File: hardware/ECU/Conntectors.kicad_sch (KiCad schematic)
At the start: 1 part

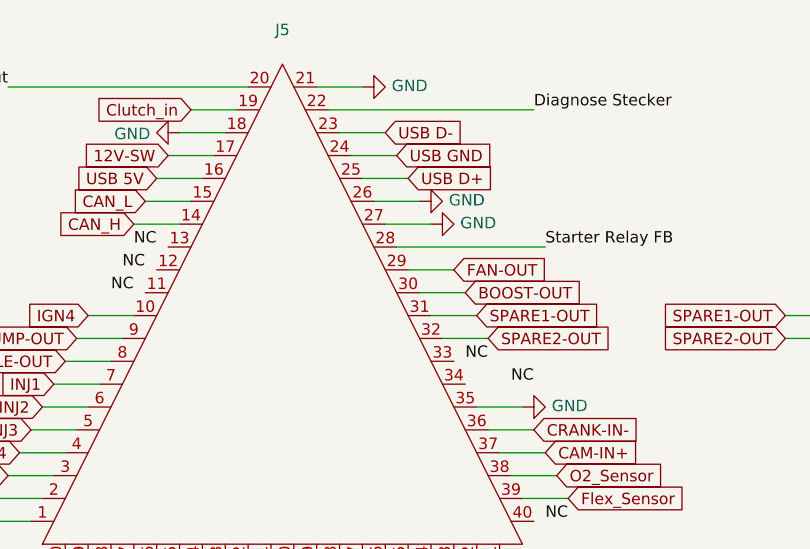
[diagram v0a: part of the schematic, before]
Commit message: Replace speeduino submodule with HasiKe fork, fix teensy.pretty path
- Switch speeduino from speeduino/speeduino to HasiKe/speeduino
- Fix teensy.pretty submodule path case mismatch (Hardware -> hardware)
- Add ISL9V5036P3-F085 component library
- Various ECU schematic updates
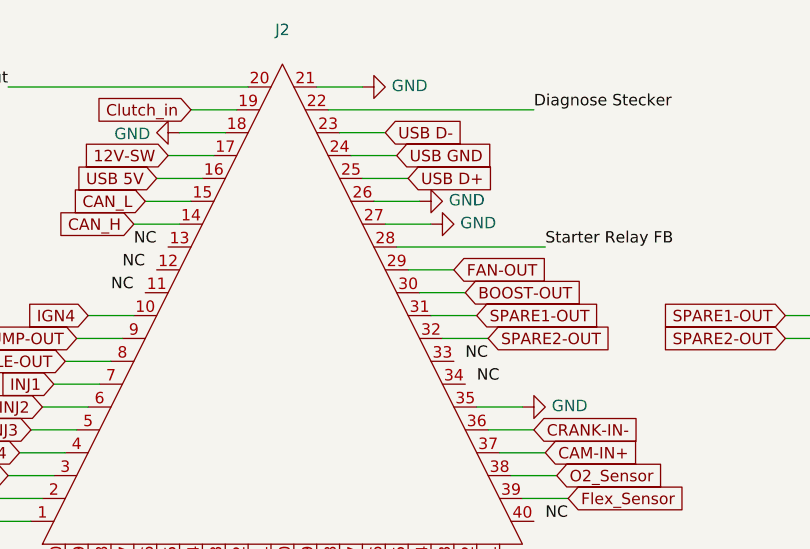
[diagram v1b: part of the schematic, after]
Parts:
- renumbered J5 to J2
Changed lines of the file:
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@@
 	)
 	(label "NC"
-		(at 173.99 99.06 0)
+		(at 170.18 99.06 0)
 		(effects
 			(font
@@
 		(on_board yes)
 		(dnp no)
-		(property "Reference" "#PWR0132"
+		(property "Reference" "#PWR031"
 			(at 181.61 101.6 0)
 			(effects
@@
 			(project "ECU"
 				(path "/aaebd8f9-fdac-426b-87c0-a208167b6035/a9903762-e61d-4762-913c-0f836ea1045d"
-					(reference "#PWR0132")
+					(reference "#PWR031")
 					(unit 1)
 				)
@@
 		(on_board yes)
 		(dnp no)
-		(property "Reference" "#PWR019"
+		(property "Reference" "#PWR028"
 			(at 163.83 66.04 0)
 			(effects
@@
 			(project "ECU"
 				(path "/aaebd8f9-fdac-426b-87c0-a208167b6035/a9903762-e61d-4762-913c-0f836ea1045d"
-					(reference "#PWR019")
+					(reference "#PWR028")
 					(unit 1)
 				)
@@
 		(on_board yes)
 		(dnp no)
-		(property "Reference" "#PWR018"
+		(property "Reference" "#PWR027"
 			(at 154.94 120.65 0)
 			(effects
@@
 			(project "ECU"
 				(path "/aaebd8f9-fdac-426b-87c0-a208167b6035/a9903762-e61d-4762-913c-0f836ea1045d"
-					(reference "#PWR018")
+					(reference "#PWR027")
 					(unit 1)
 				)
@@
 		(on_board yes)
 		(dnp no)
-		(property "Reference" "#PWR01"
+		(property "Reference" "#PWR030"
 			(at 171.45 81.28 0)
 			(effects
@@
 			(project "ECU"
 				(path "/aaebd8f9-fdac-426b-87c0-a208167b6035/a9903762-e61d-4762-913c-0f836ea1045d"
-					(reference "#PWR01")
+					(reference "#PWR030")
 					(unit 1)
 				)
@@
 		(on_board yes)
 		(dnp no)
-		(property "Reference" "#PWR020"
+		(property "Reference" "#PWR026"
 			(at 139.7 130.81 0)
 			(effects
@@
 			(project "ECU"
 				(path "/aaebd8f9-fdac-426b-87c0-a208167b6035/a9903762-e61d-4762-913c-0f836ea1045d"
-					(reference "#PWR020")
+					(reference "#PWR026")
 					(unit 1)
 				)
@@
 		(dnp no)
 		(fields_autoplaced yes)
-		(property "Reference" "J5"
+		(property "Reference" "J2"
 			(at 148.59 59.69 0)
 			(effects
@@
 			(project ""
 				(path "/aaebd8f9-fdac-426b-87c0-a208167b6035/a9903762-e61d-4762-913c-0f836ea1045d"
-					(reference "J5")
+					(reference "J2")
 					(unit 1)
 				)
@@
 		(on_board yes)
 		(dnp no)
-		(property "Reference" "#PWR017"
+		(property "Reference" "#PWR025"
 			(at 130.81 71.12 0)
 			(effects
@@
 			(project "ECU"
 				(path "/aaebd8f9-fdac-426b-87c0-a208167b6035/a9903762-e61d-4762-913c-0f836ea1045d"
-					(reference "#PWR017")
+					(reference "#PWR025")
 					(unit 1)
 				)
@@
 		(on_board yes)
 		(dnp no)
-		(property "Reference" "#PWR016"
+		(property "Reference" "#PWR029"
 			(at 170.18 78.74 0)
 			(effects
@@
 			(project "ECU"
 				(path "/aaebd8f9-fdac-426b-87c0-a208167b6035/a9903762-e61d-4762-913c-0f836ea1045d"
-					(reference "#PWR016")
+					(reference "#PWR029")
 					(unit 1)
 				)
